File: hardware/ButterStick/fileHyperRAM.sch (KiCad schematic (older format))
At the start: 3 parts, among them U4 IS66WVH16M8ALL, U5 IS66WVH16M8ALL, U6 MX25R1635

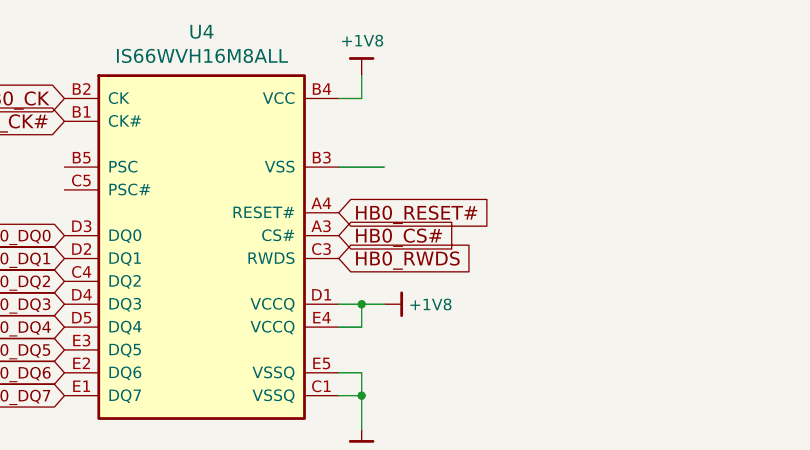
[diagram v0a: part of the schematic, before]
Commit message: Update Board.  - Added more signal breakouts  - Tidy up some pairs  - Neaten up some length matching.  - Connect RGMII
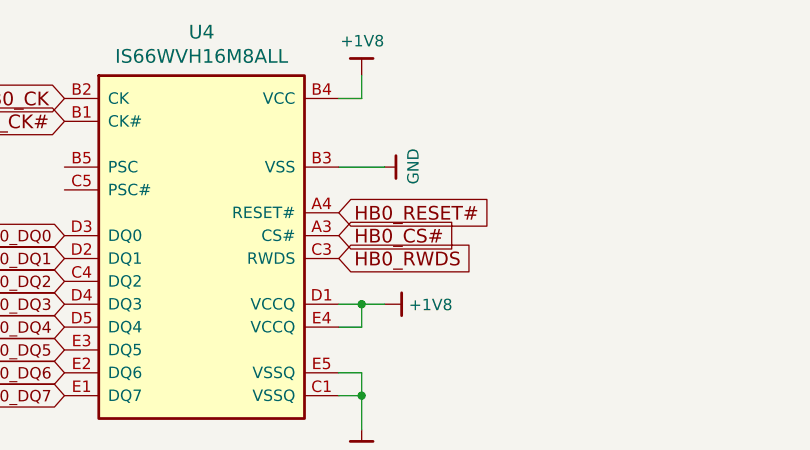
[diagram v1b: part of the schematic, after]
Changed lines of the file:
@@
 Text GLabel 7350 4300 0    50   Input ~ 0
 HB1_DQ7
+$Comp
+L gkl_power:GND #PWR?
+U 1 1 5C7E74A0
+P 4800 3300
+F 0 "#PWR?" H 4800 3050 50  0001 C CNN
+F 1 "GND" H 4803 3174 50  0000 C CNN
+F 2 "" H 4700 2950 50  0001 C CNN
+F 3 "" H 4800 3300 50  0001 C CNN
+	1    4800 3300
+	0    -1   -1   0
+$EndComp
 $EndSCHEMATC

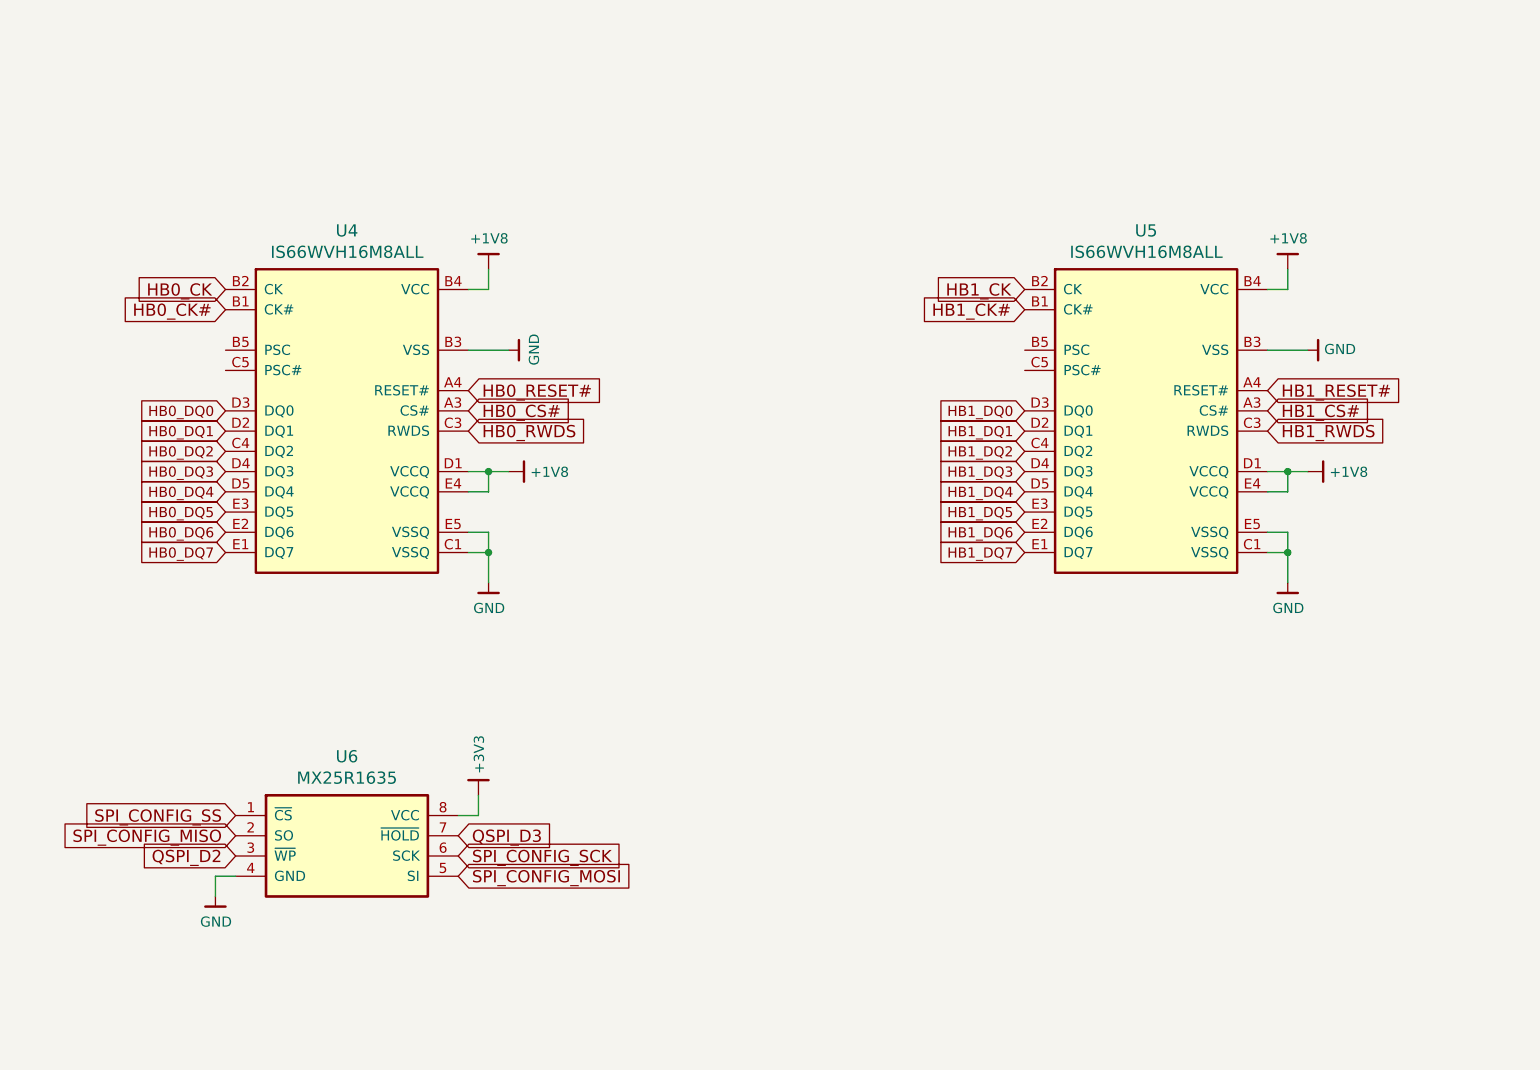
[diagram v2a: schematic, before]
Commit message: Update schematic hieracy layout.
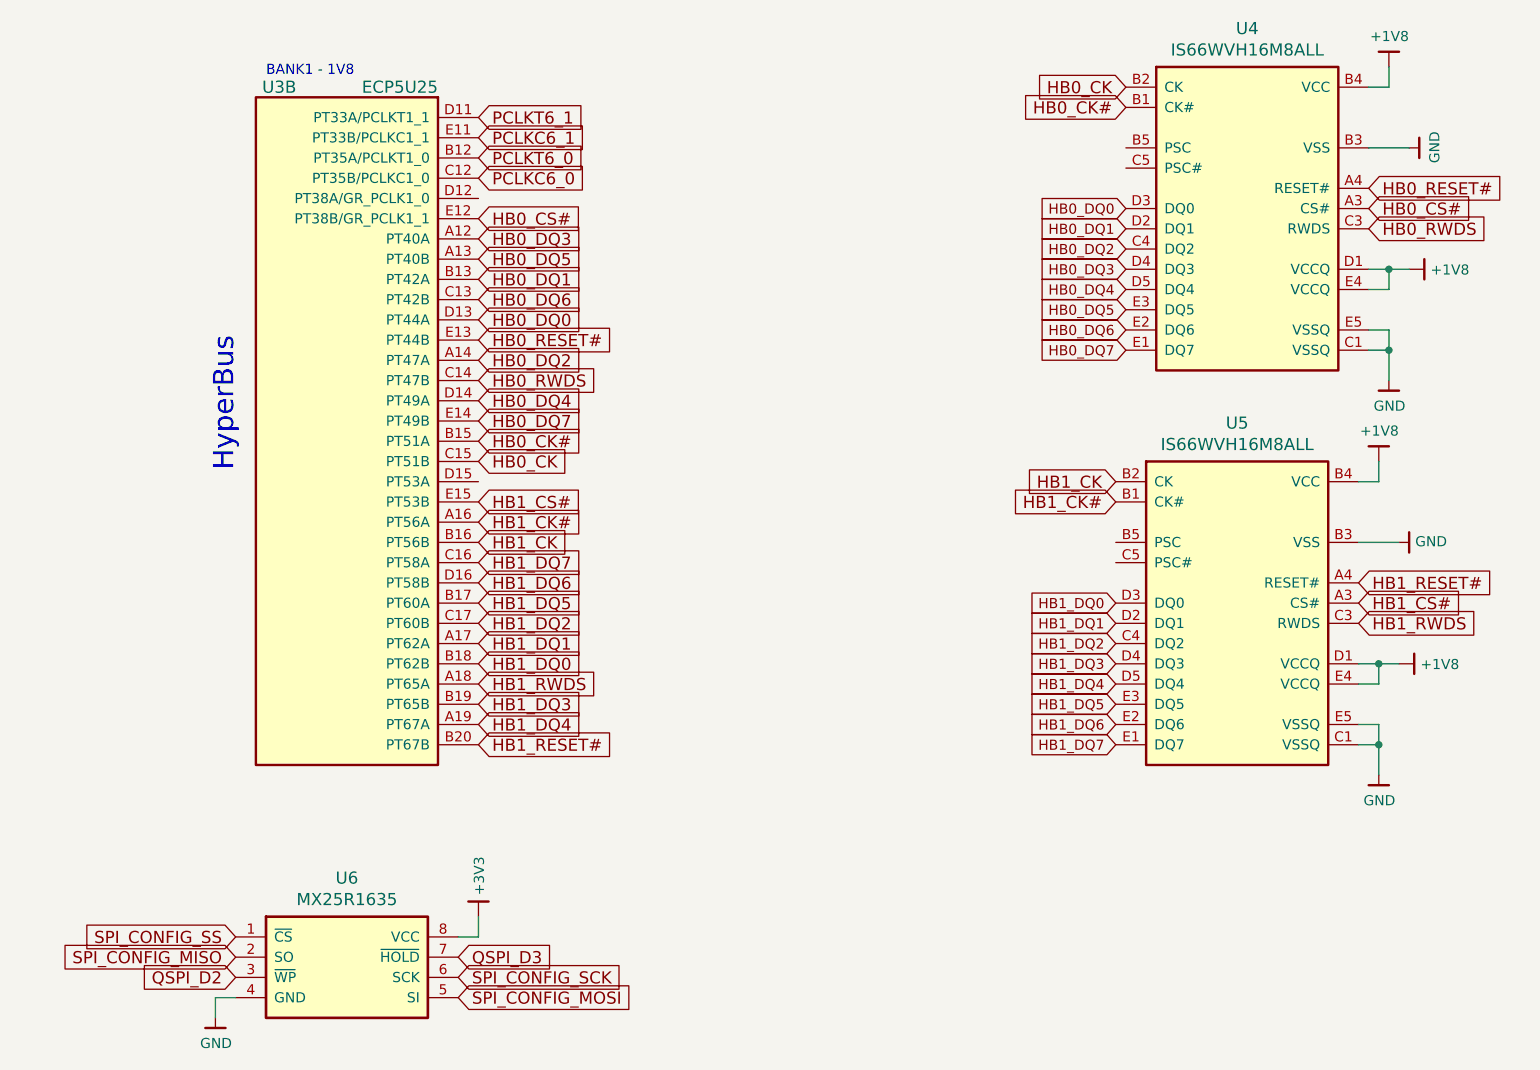
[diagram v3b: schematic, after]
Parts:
- added U3: ECP5U25, symbol gkl_lattice:ECP5U25-BG381
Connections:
- net HB0_CK: now also U3.C15 (PT51B)
- net HB0_CK#: now also U3.B15 (PT51A)
- net HB0_CS#: now also U3.E12 (PT38B/GR_PCLK1_1)
- net HB0_DQ0: now also U3.D13 (PT44A)
- net HB0_DQ1: now also U3.B13 (PT42A)
- net HB0_DQ2: now also U3.A14 (PT47A)
- net HB0_DQ3: now also U3.A12 (PT40A)
- net HB0_DQ4: now also U3.D14 (PT49A)
- net HB0_DQ5: now also U3.A13 (PT40B)
- net HB0_DQ6: now also U3.C13 (PT42B)
- net HB0_DQ7: now also U3.E14 (PT49B)
- net HB0_RESET#: now also U3.E13 (PT44B)
- net HB0_RWDS: now also U3.C14 (PT47B)
- net HB1_CK: now also U3.B16 (PT56B)
- net HB1_CK#: now also U3.A16 (PT56A)
- net HB1_CS#: now also U3.E15 (PT53B)
- net HB1_DQ0: now also U3.B18 (PT62B)
- net HB1_DQ1: now also U3.A17 (PT62A)
- net HB1_DQ2: now also U3.C17 (PT60B)
- net HB1_DQ3: now also U3.B19 (PT65B)
- net HB1_DQ4: now also U3.A19 (PT67A)
- net HB1_DQ5: now also U3.B17 (PT60A)
- net HB1_DQ6: now also U3.D16 (PT58B)
- net HB1_DQ7: now also U3.C16 (PT58A)
- net HB1_RESET#: now also U3.B20 (PT67B)
- net HB1_RWDS: now also U3.A18 (PT65A)
- new net PCLKC6_0: U3.C12 (PT35B/PCLKC1_0)
- new net PCLKC6_1: U3.E11 (PT33B/PCLKC1_1)
- new net PCLKT6_0: U3.B12 (PT35A/PCLKT1_0)
- new net PCLKT6_1: U3.D11 (PT33A/PCLKT1_1)
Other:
- note added: "BANK1 - 1V8"
- note added: "HyperBus"
- moved on the sheet: U4, U5, U6

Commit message: Routed all SYZYGY ports. Placed decoupling caps etc.
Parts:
- U3: footprint (none) -> gkl_housings_bga:caBGA_381_17x17
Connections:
- net PCLKC6_0: no longer names the net of U3.C12 (PT35B/PCLKC1_0)
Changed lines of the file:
@@
 $Descr A4 11693 8268
 encoding utf-8
-Sheet 3 13
+Sheet 3 14
 Title ""
 Date ""
@@
 Text GLabel 4650 4950 2    60   Input ~ 0
 HB1_RWDS
-Text GLabel 4650 2450 2    60   Input ~ 0
-PCLKC6_0
 Text GLabel 4650 2350 2    60   Input ~ 0
 PCLKT6_0
@@
 F 0 "U3" H 5550 2300 60  0000 L CNN
 F 1 "ECP5U25" H 4850 2300 60  0000 L CNN
-F 2 "" H 4650 2150 50  0001 C CNN
+F 2 "gkl_housings_bga:caBGA_381_17x17" H 4650 2150 50  0001 C CNN
 F 3 "" H 4650 2150 50  0001 C CNN
 F 4 " 220-2052-ND " H 800 1300 50  0001 C CNN "SN-DK"

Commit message: Switch FLASH to SO-8W footprint. Updated Routing of some componests. Re-arrange VCCIO power supplies.
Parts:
- U6: footprint Housings_DFN_QFN:DFN-8-1EP_3x2mm_Pitch0.5mm -> Package_SO:SOIJ-8_5.3x5.3mm_P1.27mm
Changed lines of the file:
@@
 F 0 "U6" H 4000 6791 60  0000 C CNN
 F 1 "MX25R1635" H 4000 6685 60  0000 C CNN
-F 2 "Housings_DFN_QFN:DFN-8-1EP_3x2mm_Pitch0.5mm" H 4000 6800 60  0001 C CNN
+F 2 "Package_SO:SOIJ-8_5.3x5.3mm_P1.27mm" H 4000 6800 60  0001 C CNN
 F 3 "" H 4000 6800 60  0001 C CNN
 F 4 "1092-1178-1-ND" H -150 2400 50  0001 C CNN "SN-DK"

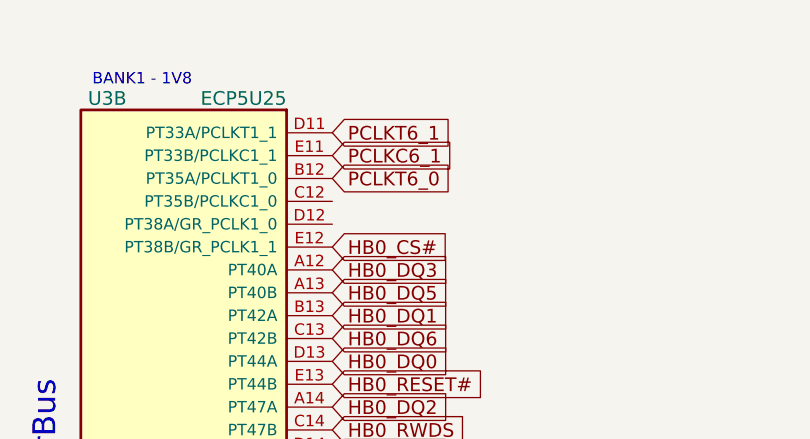
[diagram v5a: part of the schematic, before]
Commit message: Added ESD on SD card signals.
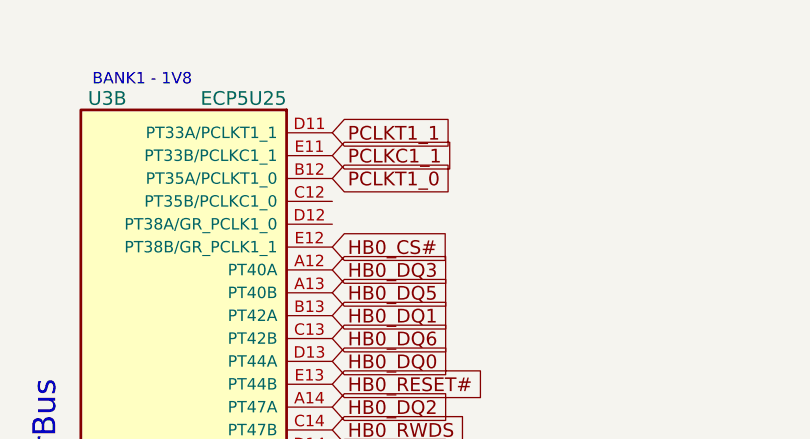
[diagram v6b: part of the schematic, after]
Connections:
- net PCLKC6_1 renamed PCLKC1_1
- net PCLKT6_0 renamed PCLKT1_0
- net PCLKT6_1 renamed PCLKT1_1
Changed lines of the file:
@@
 $Descr A4 11693 8268
 encoding utf-8
-Sheet 3 14
+Sheet 3 13
 Title ""
 Date ""
@@
 HB1_RWDS
 Text GLabel 4650 2350 2    60   Input ~ 0
-PCLKT6_0
+PCLKT1_0
 Text GLabel 4650 2250 2    60   Input ~ 0
-PCLKC6_1
+PCLKC1_1
 Text GLabel 4650 2150 2    60   Input ~ 0
-PCLKT6_1
+PCLKT1_1
 $Comp
 L gkl_lattice:ECP5U25-BG381 U?

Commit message: Update KiCad PCB.
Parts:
- U3: PN LFE5U-25F-6BG381I -> LFE5U-45F-8BG381C
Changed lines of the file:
@@
 F 3 "" H 4650 2150 50  0001 C CNN
 F 4 " 220-2052-ND " H 800 1300 50  0001 C CNN "SN-DK"
-F 5 " LFE5U-25F-6BG381I " H 800 1300 50  0001 C CNN "PN"
+F 5 "LFE5U-45F-8BG381C" H 800 1300 50  0001 C CNN "PN"
 F 6 "Lattice" H 800 1300 50  0001 C CNN "Mfg"
 	2    4650 2150

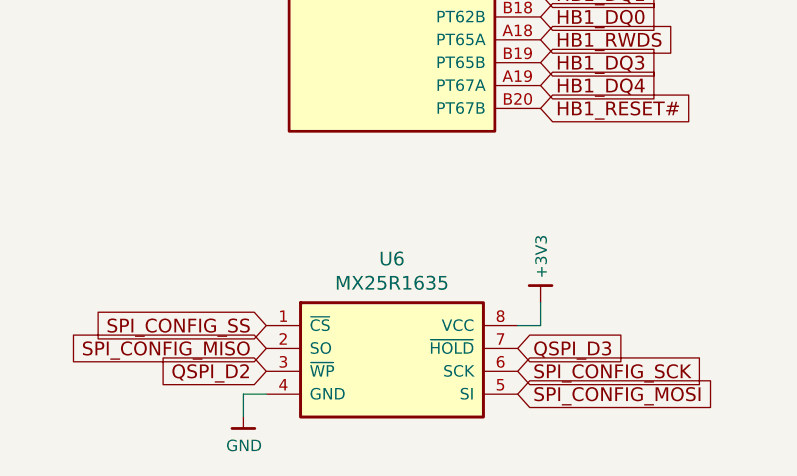
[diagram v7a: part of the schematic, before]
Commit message: Finalised part values update BOM values to reflect. Swapped layers 4/5 due to stackup changes
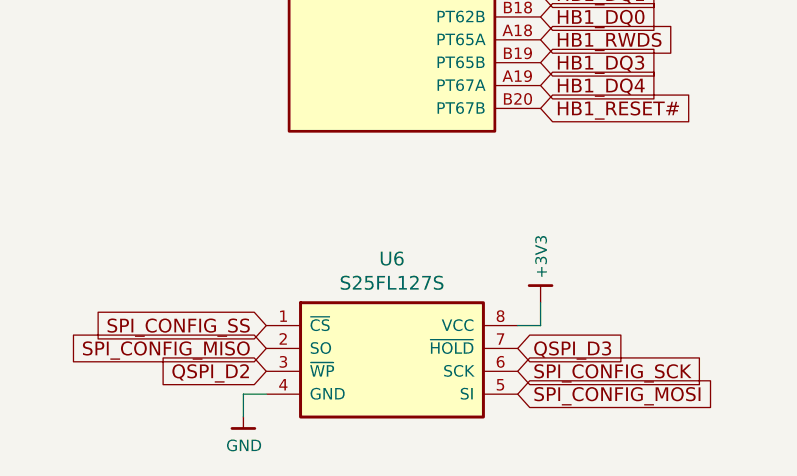
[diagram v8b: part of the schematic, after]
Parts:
- U4, U5: Mfg (none) -> ISSI, Integrated Silicon Solution Inc
- U6: value MX25R1635 -> S25FL127S; Mfg (none) -> Cypress Semiconductor Corp; PN MX25R1635FZUIH0 -> S25FL127SABMFI101
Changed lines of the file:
@@
 EESchema Schematic File Version 4
 LIBS:ButterStick-cache
-EELAYER 26 0
+EELAYER 29 0
 EELAYER END
 $Descr A4 11693 8268
 encoding utf-8
-Sheet 3 13
-Title ""
-Date ""
-Rev ""
-Comp ""
+Sheet 13 13
+Title "ButterStick"
+Date "2019-03-19"
+Rev "r0_1"
+Comp "GsD"
 Comment1 ""
 Comment2 ""
@@
 F 4 "706-1548-ND" H 500 -1250 50  0001 C CNN "SN-DK"
 F 5 "IS66WVH16M8ALL-166B1LI" H 500 -1250 50  0001 C CNN "PN"
+F 6 "ISSI, Integrated Silicon Solution Inc" H 0   0   50  0001 C CNN "Mfg"
 	1    8450 2650
 	1    0    0    -1
@@
 P 4000 6350
 F 0 "U6" H 4000 6791 60  0000 C CNN
-F 1 "MX25R1635" H 4000 6685 60  0000 C CNN
+F 1 "S25FL127S" H 4000 6685 60  0000 C CNN
 F 2 "Package_SO:SOIJ-8_5.3x5.3mm_P1.27mm" H 4000 6800 60  0001 C CNN
 F 3 "" H 4000 6800 60  0001 C CNN
 F 4 "1092-1178-1-ND" H -150 2400 50  0001 C CNN "SN-DK"
-F 5 "MX25R1635FZUIH0" H -150 2400 50  0001 C CNN "PN"
+F 5 "S25FL127SABMFI101" H -150 2400 50  0001 C CNN "PN"
+F 6 "Cypress Semiconductor Corp" H 0   0   50  0001 C CNN "Mfg"
 	1    4000 6350
 	1    0    0    -1
@@
 F 4 "706-1548-ND" H 450 700 50  0001 C CNN "SN-DK"
 F 5 "IS66WVH16M8ALL-166B1LI" H 450 700 50  0001 C CNN "PN"
+F 6 "ISSI, Integrated Silicon Solution Inc" H 0   0   50  0001 C CNN "Mfg"
 	1    8400 4600
 	1    0    0    -1
